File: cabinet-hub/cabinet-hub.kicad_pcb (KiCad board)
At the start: 2 copper layers, 46.4 x 37.5 mm, 15 parts

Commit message: Update hub
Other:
- board text added: "FAJRAN 2016"
- board text added: "REV 01"
- board text removed: "fajran 2016"
- board text removed: "rev01"
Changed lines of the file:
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@@
     (links 27)
     (no_connects 0)
-    (area 144.069999 65.329999 190.575001 102.945001)
+    (area 144.069999 64.29 190.575001 103.365)
     (thickness 1.6)
     (drawings 11)
@@
       (xy -0.113933 2.757629) (xy -0.013056 2.757714) (xy 0 2.757714) (xy 0.10391 2.757652)) (layer B.SilkS) (width 0.01))
   )
-  (gr_text rev01 (at 154.305 100.965) (layer B.SilkS)
+  (gr_text "REV 01" (at 153.543 101.092) (layer B.SilkS)
     (effects (font (size 1 1) (thickness 0.1)) (justify right mirror))
   )
-  (gr_text "fajran 2016" (at 180.975 100.965) (layer B.SilkS)
+  (gr_text "FAJRAN 2016" (at 180.975 101.092) (layer B.SilkS)
     (effects (font (size 1 1) (thickness 0.1)) (justify left mirror))
   )

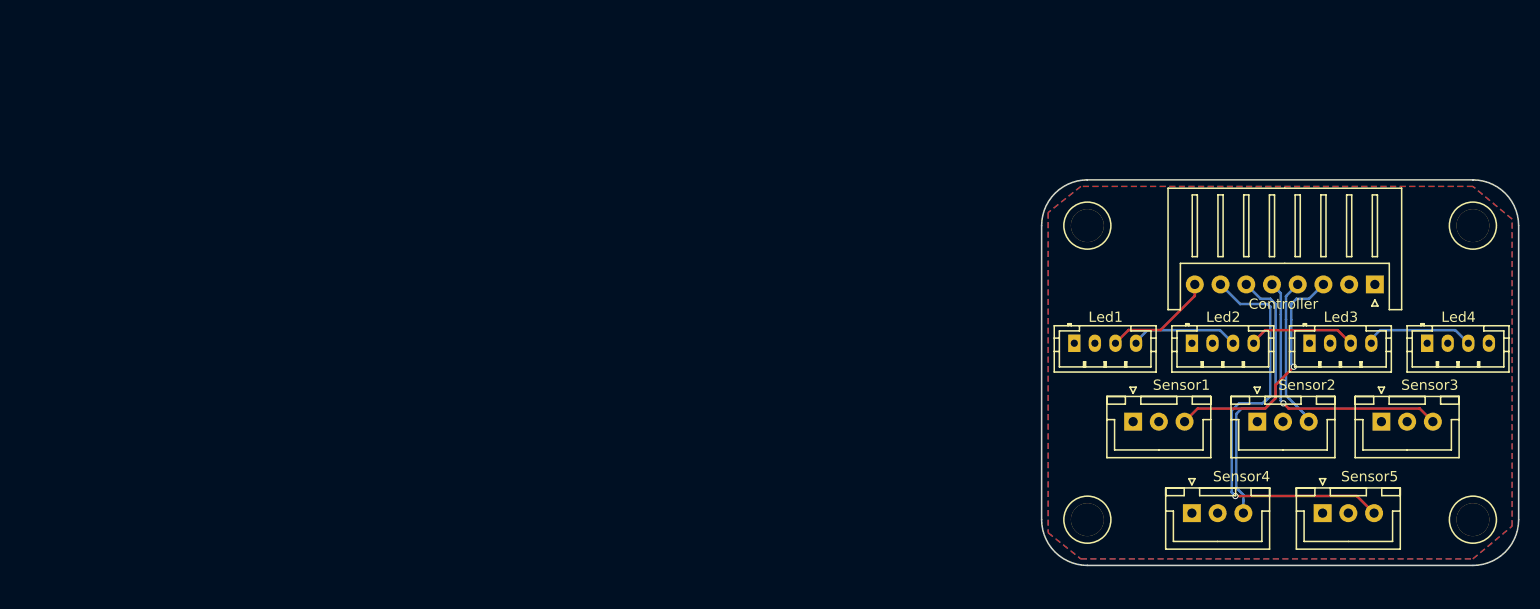
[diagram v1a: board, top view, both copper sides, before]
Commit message: Add more LED port
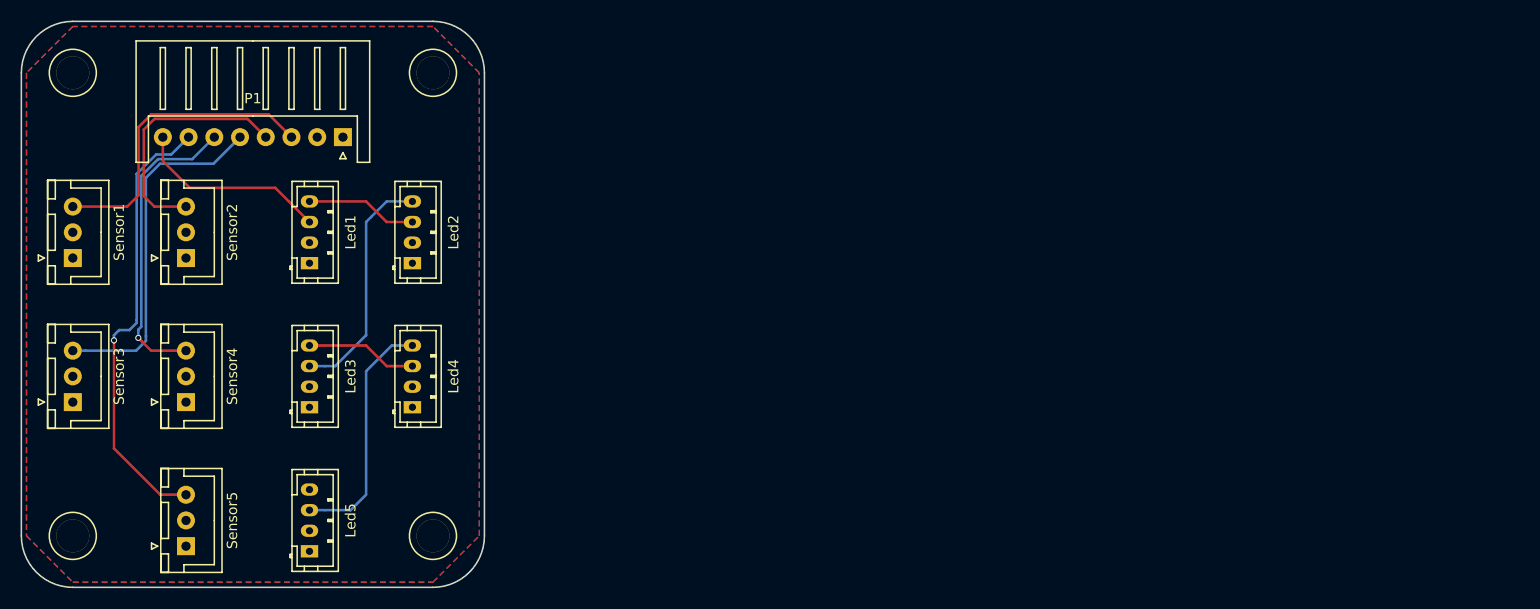
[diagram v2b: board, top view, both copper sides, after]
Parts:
- removed Controller: Controller, Connectors_JST:JST_XH_S08B-XH-A_08x2.50mm_Angled
- removed Led1: Led1, Connectors_JST:JST_PH_B4B-PH-K_04x2.00mm_Straight
- removed Led2: Led2, Connectors_JST:JST_PH_B4B-PH-K_04x2.00mm_Straight
- removed Led3: Led3, Connectors_JST:JST_PH_B4B-PH-K_04x2.00mm_Straight
- removed Led4: Led4, Connectors_JST:JST_PH_B4B-PH-K_04x2.00mm_Straight
- removed REF***: OSHW-Logo2_7.3x6mm_SilkScreen, Symbols:OSHW-Logo2_7.3x6mm_SilkScreen
- removed Sensor1: Sensor1, Connectors_JST:JST_XH_B03B-XH-A_03x2.50mm_Straight
- removed Sensor2: Sensor2, Connectors_JST:JST_XH_B03B-XH-A_03x2.50mm_Straight
- removed Sensor3: Sensor3, Connectors_JST:JST_XH_B03B-XH-A_03x2.50mm_Straight
- removed Sensor4: Sensor4, Connectors_JST:JST_XH_B03B-XH-A_03x2.50mm_Straight
- removed Sensor5: Sensor5, Connectors_JST:JST_XH_B03B-XH-A_03x2.50mm_Straight
- added P1: Controller, Connectors_JST:JST_XH_S08B-XH-A_08x2.50mm_Angled, F.Cu at (76.2, 61.2)
- added P10: Led4, Connectors_JST:JST_PH_B4B-PH-K_04x2.00mm_Straight, F.Cu at (83.0, 87.5)
- added P11: Led5, Connectors_JST:JST_PH_B4B-PH-K_04x2.00mm_Straight, F.Cu at (73.0, 101.5)
- added P2: Sensor1, Connectors_JST:JST_XH_B03B-XH-A_03x2.50mm_Straight, F.Cu at (50.0, 73.0)
- added P3: Sensor2, Connectors_JST:JST_XH_B03B-XH-A_03x2.50mm_Straight, F.Cu at (61.0, 73.0)
- added P4: Sensor3, Connectors_JST:JST_XH_B03B-XH-A_03x2.50mm_Straight, F.Cu at (50.0, 87.0)
- added P5: Sensor4, Connectors_JST:JST_XH_B03B-XH-A_03x2.50mm_Straight, F.Cu at (61.0, 87.0)
- added P6: Sensor5, Connectors_JST:JST_XH_B03B-XH-A_03x2.50mm_Straight, F.Cu at (61.0, 101.0)
- added P7: Led1, Connectors_JST:JST_PH_B4B-PH-K_04x2.00mm_Straight, F.Cu at (73.0, 73.5)
- added P8: Led2, Connectors_JST:JST_PH_B4B-PH-K_04x2.00mm_Straight, F.Cu at (83.0, 73.5)
- added P9: Led3, Connectors_JST:JST_PH_B4B-PH-K_04x2.00mm_Straight, F.Cu at (73.0, 87.5)
- moved REF** 102.1 mm to (85.0, 55.0)
- moved REF** 101.1 mm to (85.0, 100.0)
- moved REF** 99.7 mm to (50.0, 55.0)
- moved REF** 98.6 mm to (50.0, 100.0)
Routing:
- net /Led-4-5: track 0.00 -> 23.7 mm
- net /Led-2-3: track 10.6 -> 23.6 mm
- net /In2: track 14.9 -> 24.0 mm
- net /Led-1: track 10.7 -> 19.0 mm
- net /In3: track 27.5 -> 34.1 mm, vias 1 -> 0
- net /In1: track 24.0 -> 29.8 mm, vias 1 -> 0
- net /In5: track 41.8 -> 43.6 mm
- net /In4: track 27.9 -> 29.7 mm, vias 0 -> 1
- added copper zone on F.Cu, net +5V
- added copper zone on B.Cu, net GND
- removed copper zone on B.Cu, net +5V
- removed copper zone on F.Cu, net GND
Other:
- board size 46.4 x 37.5 mm -> 45 x 55 mm
